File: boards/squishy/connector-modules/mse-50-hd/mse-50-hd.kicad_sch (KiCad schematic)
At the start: 14 parts, among them J1 SCSI PHY Mezz, J3 Conn_01x04, J5 HD 50, U1 M24C02-RMC

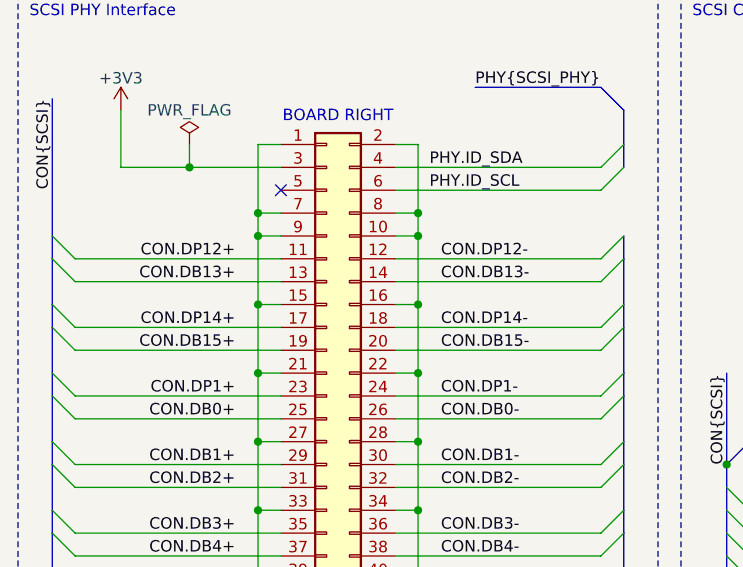
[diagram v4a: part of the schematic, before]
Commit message: squishy: connectors: s/DP12/DB12/g s/DP14/DB14/g
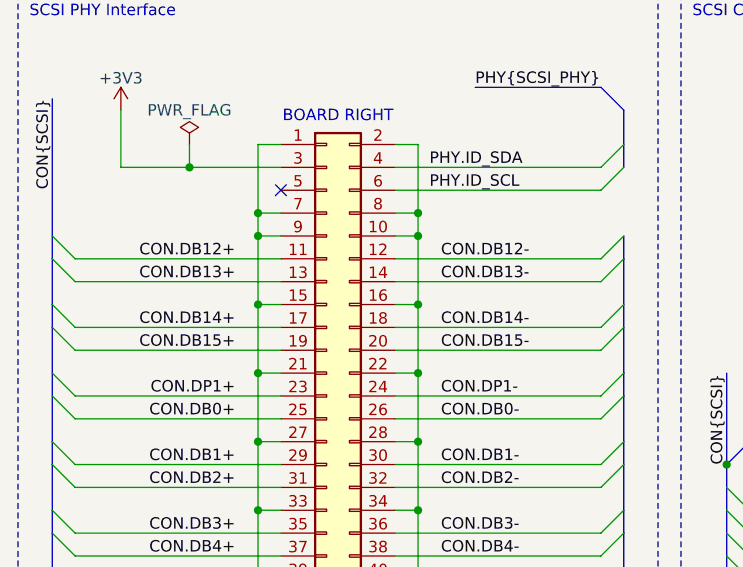
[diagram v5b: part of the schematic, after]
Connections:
- net CON.DP12+ renamed CON.DB12+
- net CON.DP12- renamed CON.DB12-
- net CON.DP14+ renamed CON.DB14+
- net CON.DP14- renamed CON.DB14-
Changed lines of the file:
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@@
 		)
 	)
-	(label "CON.DP14-"
+	(label "CON.DB14-"
 		(at 60.96 52.07 0)
 		(fields_autoplaced yes)
@@
 		)
 	)
-	(label "CON.DP12+"
+	(label "CON.DB12+"
 		(at 38.1 44.45 180)
 		(fields_autoplaced yes)
@@
 		)
 	)
-	(label "CON.DP12-"
+	(label "CON.DB12-"
 		(at 60.96 44.45 0)
 		(fields_autoplaced yes)
@@
 		)
 	)
-	(label "CON.DP14+"
+	(label "CON.DB14+"
 		(at 38.1 52.07 180)
 		(fields_autoplaced yes)

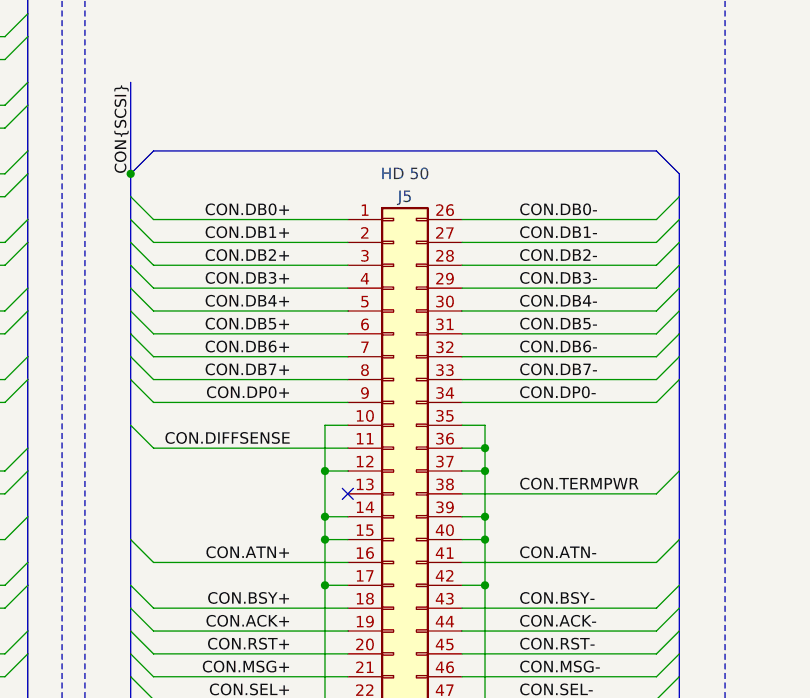
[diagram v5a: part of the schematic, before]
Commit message: squishy: connectors: updated SCSI connector metadata for mse-50-hd
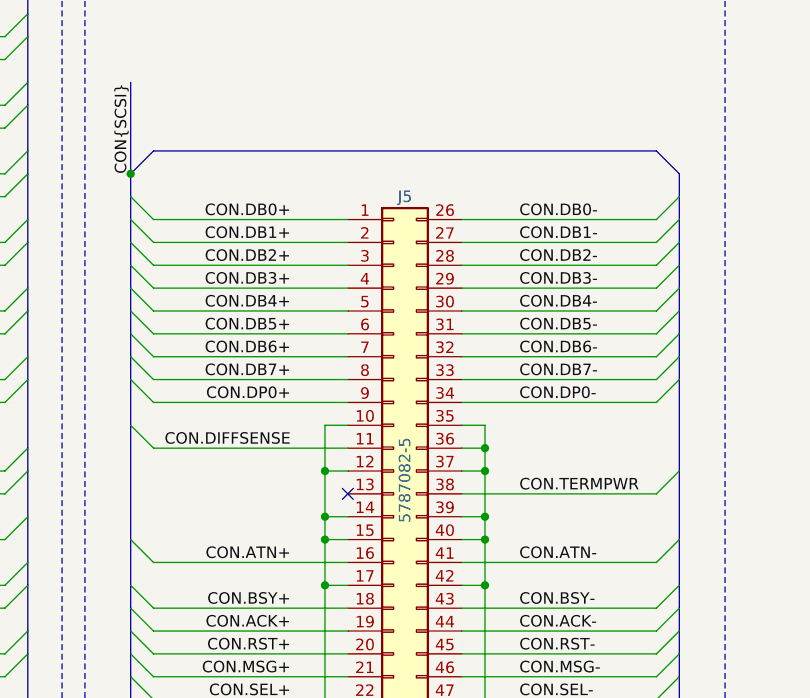
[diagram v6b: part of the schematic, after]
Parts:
- J5: value HD 50 -> 5787082-5; MFR (none) -> TE Connectivity; MPN (none) -> 5787082-5; URL (none) -> https://www.te.com/en/product-5787082-5.html
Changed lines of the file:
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@@
 			)
 		)
-		(property "Value" "HD 50"
-			(at 123.19 67.31 0)
+		(property "Value" "5787082-5"
+			(at 123.19 101.346 90)
 			(effects
 				(font
@@
 			)
 		)
-		(property "Datasheet" "~"
+		(property "Datasheet" "https://www.te.com/commerce/DocumentDelivery/DDEController?Action=showdoc&DocId=Specification+Or+Standard%7F114-40029%7FJ%7Fpdf%7FEnglish%7FENG_SS_114-40029_J.pdf%7F5787082-5"
 			(at 121.92 120.65 0)
 			(effects
@@
 			)
 		)
-		(property "Description" "Generic connector, double row, 02x25, counter clockwise pin numbering scheme (similar to DIP package numbering), with shielding"
+		(property "Description" "AMPLITE 1.27mm High-density D-subminiature 50-pin connector"
 			(at 123.19 101.6 0)
 			(effects
+				(font
+					(size 1.27 1.27)
+				)
+				(hide yes)
+			)
+		)
+		(property "MFR" "TE Connectivity"
+			(at 123.19 101.6 0)
+			(effects
+				(font
+					(size 1.27 1.27)
+				)
+				(hide yes)
+			)
+		)
+		(property "MPN" "5787082-5"
+			(at 123.19 101.6 0)
+			(effects
+				(font
+					(size 1.27 1.27)
+				)
+				(hide yes)
+			)
+		)
+		(property "URL" "https://www.te.com/en/product-5787082-5.html"
+			(at 123.19 101.6 0)
+			(effects

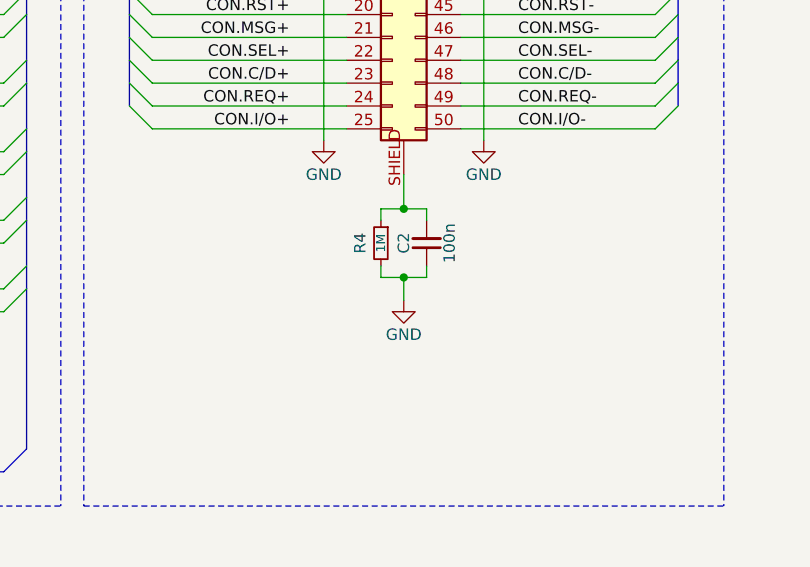
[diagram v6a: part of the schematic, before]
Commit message: squishy: connectors: Routed and length matched the mse-50-hd connector interface
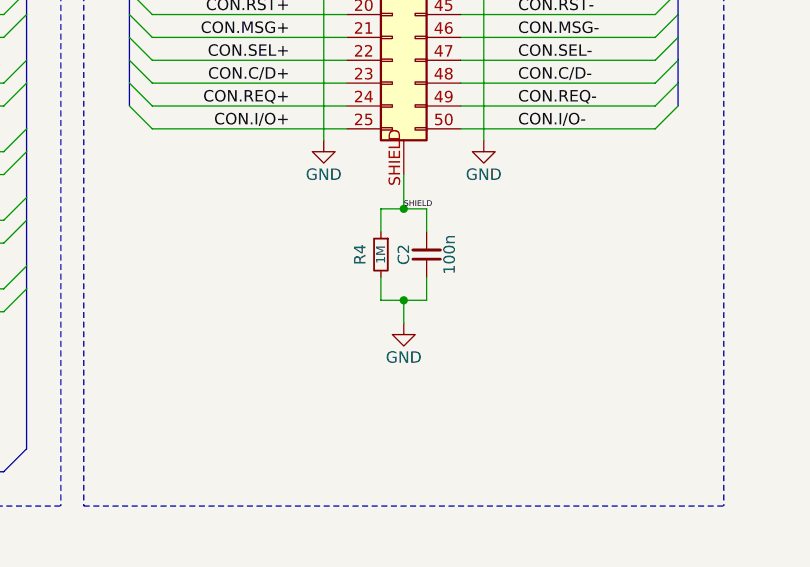
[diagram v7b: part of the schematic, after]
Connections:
- net SHIELD: now reaches C2.2, J5.SHIELD, R4.1
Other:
- moved on the sheet: C2, R4
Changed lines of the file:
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@@
 	)
 	(junction
-		(at 123.19 149.86)
+		(at 123.19 152.4)
 		(diameter 0)
 		(color 0 0 0 0)
@@
 	(wire
 		(pts
-			(xy 125.73 148.59) (xy 125.73 149.86)
+			(xy 125.73 149.86) (xy 125.73 152.4)
 		)
 		(stroke
@@
 	(wire
 		(pts
-			(xy 125.73 143.51) (xy 125.73 142.24)
+			(xy 125.73 144.78) (xy 125.73 142.24)
 		)
 		(stroke
@@
 	(wire
 		(pts
-			(xy 120.65 143.51) (xy 120.65 142.24)
+			(xy 120.65 144.78) (xy 120.65 142.24)
 		)
 		(stroke
@@
 	(wire
 		(pts
-			(xy 120.65 149.86) (xy 123.19 149.86)
+			(xy 120.65 152.4) (xy 123.19 152.4)
 		)
 		(stroke
@@
 	(wire
 		(pts
-			(xy 123.19 152.4) (xy 123.19 149.86)
+			(xy 123.19 154.94) (xy 123.19 152.4)
 		)
 		(stroke
@@
 		)
 	)
+	(wire
+		(pts
+			(xy 120.65 149.86) (xy 120.65 152.4)
+		)
+		(stroke
+			(width 0)
+			(type default)
+		)
+	)
 	(bus
 		(pts
@@
 	(wire
 		(pts
-			(xy 120.65 148.59) (xy 120.65 149.86)
-		)
-		(stroke
-			(width 0)
-			(type default)
-		)
-	)
-	(wire
-		(pts
 			(xy 43.18 49.53) (xy 40.64 49.53)
 		)
@@
 	(wire
 		(pts
-			(xy 123.19 149.86) (xy 125.73 149.86)
+			(xy 123.19 152.4) (xy 125.73 152.4)
 		)
 		(stroke
@@
 		)
 	)
+	(label "SHIELD"
+		(at 123.19 142.24 0)
+		(fields_autoplaced yes)
+		(effects
+			(font
+				(size 0.635 0.635)
+			)
+			(justify left bottom)
+		)
+	)
 	(label "CON.DB13+"
 		(at 38.1 46.99 180)
@@
 	(symbol
 		(lib_id "Device:C_Small")
-		(at 125.73 146.05 180)
+		(at 125.73 147.32 180)
 		(unit 1)
 		(exclude_from_sim no)
@@
 		(dnp no)
 		(property "Reference" "C2"
-			(at 123.19 146.05 90)
+			(at 123.19 147.32 90)
 			(effects
 				(font
@@
 		)
 		(property "Value" "100n"
-			(at 128.27 146.05 90)
+			(at 128.27 147.32 90)
 			(effects
 				(font
@@
 		)
 		(property "Footprint" "rhais_rcl:C0603"
-			(at 125.73 146.05 0)
+			(at 125.73 147.32 0)
 			(effects
 				(font
@@
 		)
 		(property "Datasheet" "https://content.kemet.com/datasheets/KEM_C1006_X5R_SMD.pdf"
-			(at 125.73 146.05 0)
+			(at 125.73 147.32 0)
 			(effects
 				(font
@@
 		)
 		(property "Description" ""
-			(at 125.73 146.05 0)
+			(at 125.73 147.32 0)
 			(effects
 				(font
@@
 		)
 		(property "MFR" "KEMET"
-			(at 125.73 146.05 90)
+			(at 125.73 147.32 90)
 			(effects
 				(font
@@
 		)
 		(property "MPN" "C0603C104M5RACTU"
-			(at 125.73 146.05 90)
+			(at 125.73 147.32 90)
 			(effects
 				(font
@@
 		)
 		(property "Tolerance" "±20% 50V"
-			(at 125.73 146.05 0)
+			(at 125.73 147.32 0)
 			(effects
 				(font
@@
 		)
 		(property "SUPPLIER" "DigiKey"
-			(at 125.73 146.05 0)
+			(at 125.73 147.32 0)
 			(effects
 				(font
@@
 		)
 		(property "SUPPLIER_OC" "399-C0603C104M5RAC7867DKR-ND"
-			(at 125.73 146.05 0)
+			(at 125.73 147.32 0)
 			(effects
 				(font
@@
 		)
 		(property "SUPPLIER_URL" "https://www.digikey.com/short/8nqzrr4b"
-			(at 125.73 146.05 0)
+			(at 125.73 147.32 0)
 			(effects
 				(font
@@
 	(symbol
 		(lib_id "Device:R_Small")
-		(at 120.65 146.05 0)
+		(at 120.65 147.32 0)
 		(mirror y)
 		(unit 1)
@@
 		(dnp no)
 		(property "Reference" "R4"
-			(at 117.602 146.05 90)
+			(at 117.602 147.32 90)
 			(effects
 				(font
@@
 		)
 		(property "Value" "1M"
-			(at 120.65 146.05 90)
+			(at 120.65 147.32 90)
 			(effects
 				(font
@@
 		)
 		(property "Footprint" "rhais_rcl:R0603"
-			(at 120.65 146.05 0)
+			(at 120.65 147.32 0)
 			(effects
 				(font
@@
 		)
 		(property "Datasheet" ""
-			(at 120.65 146.05 0)
+			(at 120.65 147.32 0)
 			(effects
 				(font
@@
 		)
 		(property "Description" ""
-			(at 120.65 146.05 0)
+			(at 120.65 147.32 0)
 			(effects
 				(font
@@
 		)
 		(property "MFR" ""
-			(at 120.65 146.05 90)
+			(at 120.65 147.32 90)
 			(effects
 				(font
@@
 		)
 		(property "MPN" ""
-			(at 120.65 146.05 90)
+			(at 120.65 147.32 90)
 			(effects
 				(font
@@
 		)
 		(property "Tolerance" ""
-			(at 120.65 146.05 0)
+			(at 120.65 147.32 0)
 			(effects
 				(font
@@
 		)
 		(property "SUPPLIER" "DigiKey"
-			(at 120.65 146.05 0)
+			(at 120.65 147.32 0)
 			(effects
 				(font
@@
 		)
 		(property "SUPPLIER_OC" ""
-			(at 120.65 146.05 0)
+			(at 120.65 147.32 0)
 			(effects
 				(font
@@
 		)
 		(property "SUPPLIER_URL" ""
-			(at 120.65 146.05 0)
+			(at 120.65 147.32 0)
 			(effects
 				(font
@@
 	(symbol
 		(lib_id "power:GND")
-		(at 123.19 152.4 0)
+		(at 123.19 154.94 0)
 		(mirror y)
 		(unit 1)
@@
 		(dnp no)
 		(property "Reference" "#PWR012"
-			(at 123.19 158.75 0)
+			(at 123.19 161.29 0)
 			(effects
 				(font
@@
 		)
 		(property "Value" "GND"
-			(at 123.19 156.21 0)
+			(at 123.19 158.75 0)
 			(effects
 				(font
@@
 		)
 		(property "Footprint" ""
-			(at 123.19 152.4 0)
+			(at 123.19 154.94 0)
 			(effects
 				(font
@@
 		)
 		(property "Datasheet" ""
-			(at 123.19 152.4 0)
+			(at 123.19 154.94 0)
 			(effects
 				(font
@@
 		)
 		(property "Description" "Power symbol creates a global label with name \"GND\" , ground"
-			(at 123.19 152.4 0)
+			(at 123.19 154.94 0)
 			(effects
 				(font

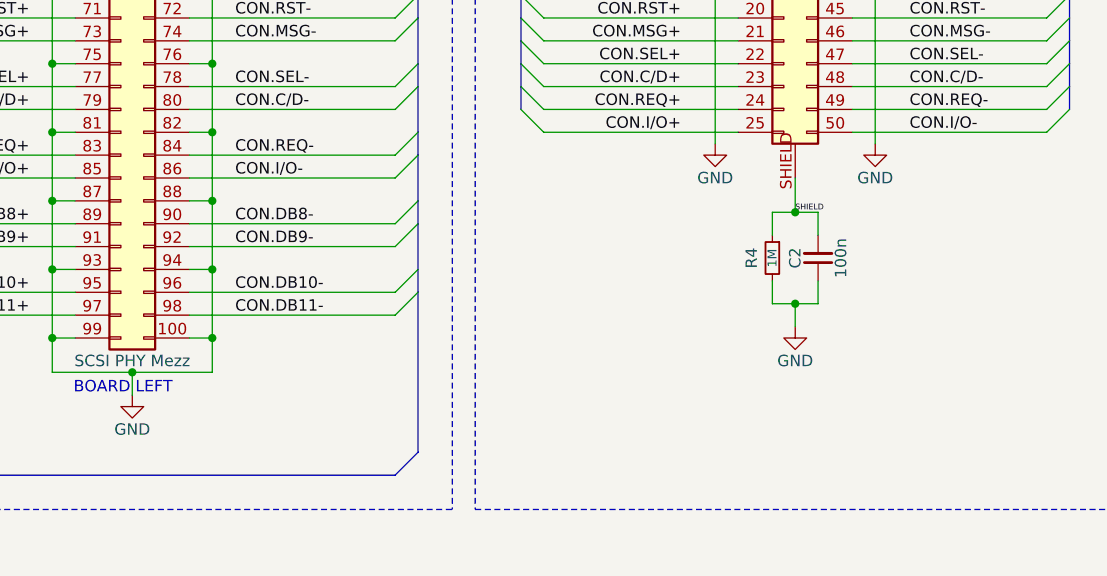
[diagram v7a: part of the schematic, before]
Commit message: squishy: connectors: Adjustments for ERC and DRC cleanliness for mse-50-hd connector interface board
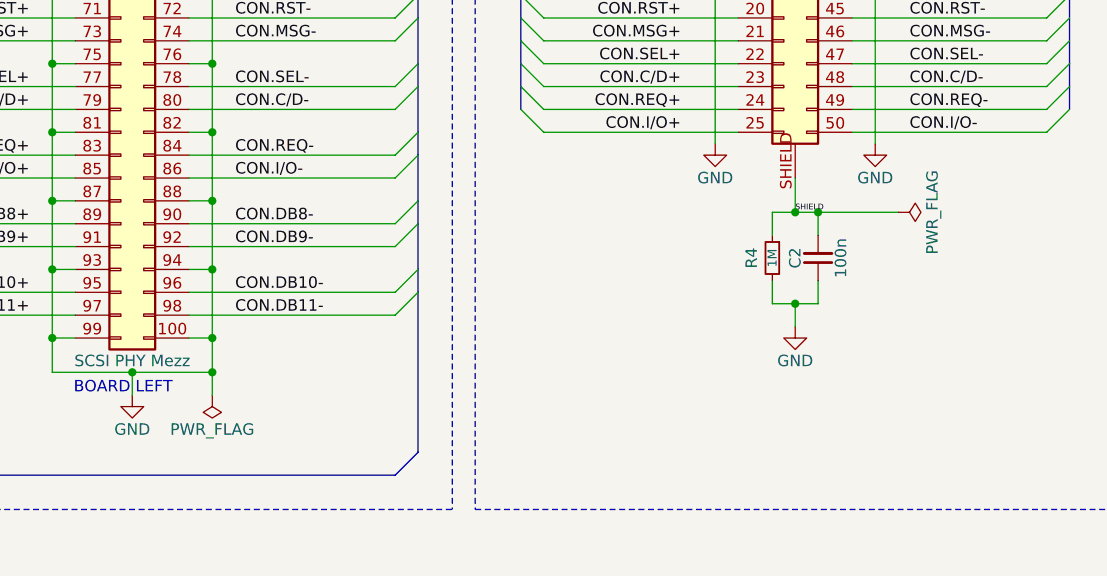
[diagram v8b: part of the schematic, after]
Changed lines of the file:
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@@
 	)
 	(junction
+		(at 125.73 142.24)
+		(diameter 0)
+		(color 0 0 0 0)
+	)
+	(junction
 		(at 114.3 105.41)
 		(diameter 0)
@@
 	)
 	(junction
+		(at 58.42 160.02)
+		(diameter 0)
+		(color 0 0 0 0)
+	)
+	(junction
 		(at 58.42 57.15)
 		(diameter 0)
@@
 	(wire
 		(pts
+			(xy 125.73 142.24) (xy 134.62 142.24)
+		)
+		(stroke
+			(width 0)
+			(type default)
+		)
+	)
+	(wire
+		(pts
 			(xy 20.32 138.43) (xy 43.18 138.43)
 		)
@@
 	(wire
 		(pts
+			(xy 58.42 160.02) (xy 58.42 162.56)
+		)
+		(stroke
+			(width 0)
+			(type default)
+		)
+	)
+	(wire
+		(pts
 			(xy 58.42 148.59) (xy 58.42 156.21)
 		)
@@
 	)
 	(symbol
+		(lib_id "power:PWR_FLAG")
+		(at 58.42 162.56 180)
+		(unit 1)
+		(exclude_from_sim no)
+		(in_bom yes)
+		(on_board yes)
+		(dnp no)
+		(property "Reference" "#FLG02"
+			(at 58.42 164.465 0)
+			(effects
+				(font
+					(size 1.27 1.27)
+				)
+				(hide yes)
+			)
+		)
+		(property "Value" "PWR_FLAG"
+			(at 58.42 166.37 0)
+			(effects
+				(font
+					(size 1.27 1.27)
+				)
+			)
+		)
+		(property "Footprint" ""
+			(at 58.42 162.56 0)
+			(effects
+				(font
+					(size 1.27 1.27)
+				)
+				(hide yes)
+			)
+		)
+		(property "Datasheet" "~"
+			(at 58.42 162.56 0)
+			(effects
+				(font
+					(size 1.27 1.27)
+				)
+				(hide yes)
+			)
+		)
+		(property "Description" "Special symbol for telling ERC where power comes from"
+			(at 58.42 162.56 0)
+			(effects
+				(font
+					(size 1.27 1.27)
+				)
+				(hide yes)
+			)
+		)
+		(pin "1"
+		)
+		(instances
+			(project "mse-50-hd"
+				(path "/bd9eafec-5355-49e4-b2e3-916daacb0a86"
+					(reference "#FLG02")
+					(unit 1)
+				)
+			)
+		)
+	)
+	(symbol
 		(lib_id "Device:C_Small")
 		(at 125.73 147.32 180)
@@
 					(unit 1)
 				)
+			)
+		)
+	)
+	(symbol
+		(lib_id "power:PWR_FLAG")
+		(at 134.62 142.24 270)
+		(unit 1)
+		(exclude_from_sim no)
+		(in_bom yes)
+		(on_board yes)
+		(dnp no)
+		(property "Reference" "#FLG03"
+			(at 136.525 142.24 0)
+			(effects
+				(font
+					(size 1.27 1.27)
+				)
+				(hide yes)
+			)
+		)
+		(property "Value" "PWR_FLAG"
+			(at 138.43 142.24 0)
+			(effects
+				(font
+					(size 1.27 1.27)
+				)
+			)
+		)
+		(property "Footprint" ""
+			(at 134.62 142.24 0)
+			(effects
+				(font
+					(size 1.27 1.27)
+				)
+				(hide yes)
+			)
+		)
+		(property "Datasheet" "~"
+			(at 134.62 142.24 0)
+			(effects
+				(font
+					(size 1.27 1.27)
+				)
+				(hide yes)
+			)
+		)
+		(property "Description" "Special symbol for telling ERC where power comes from"
+			(at 134.62 142.24 0)
+			(effects
+				(font
+					(size 1.27 1.27)
+				)
+				(hide yes)
+			)
+		)
+		(pin "1"
+		)
+		(instances
+			(project "mse-50-hd"
+				(path "/bd9eafec-5355-49e4-b2e3-916daacb0a86"
+					(reference "#FLG03")
+					(unit 1)
+				)
